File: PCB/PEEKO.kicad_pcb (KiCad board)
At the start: 2 copper layers, 52.1 x 43.2 mm, 32 parts, among them J1 Rasberry PI Pico, J2 Conn_02x15_Odd_Even, J3 Conn_01x02_Pin, J4 Conn_01x02_Pin, U1 TXU0104, U2 TXU0104, U3 TXU0104, U4 TXU0104, U5 TXU0104, U6 TXU0104

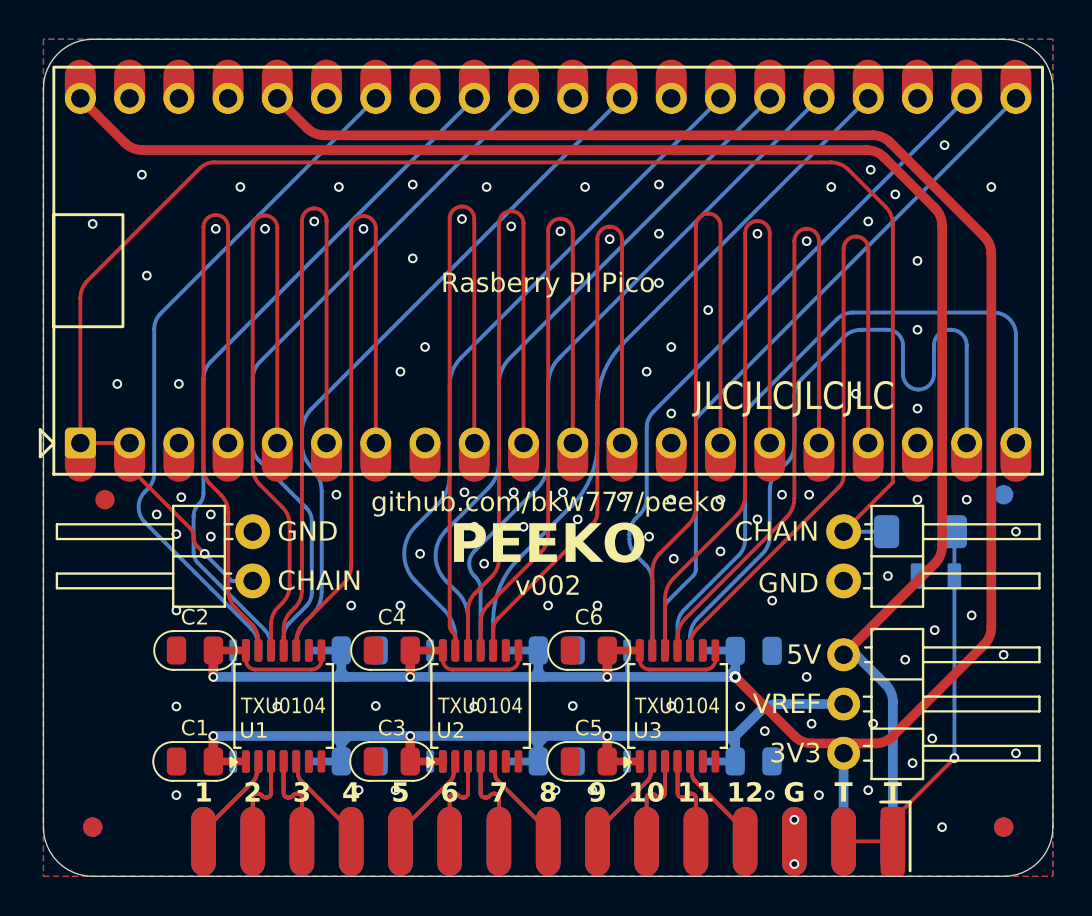
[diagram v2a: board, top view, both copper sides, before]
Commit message: local fiducial footprint
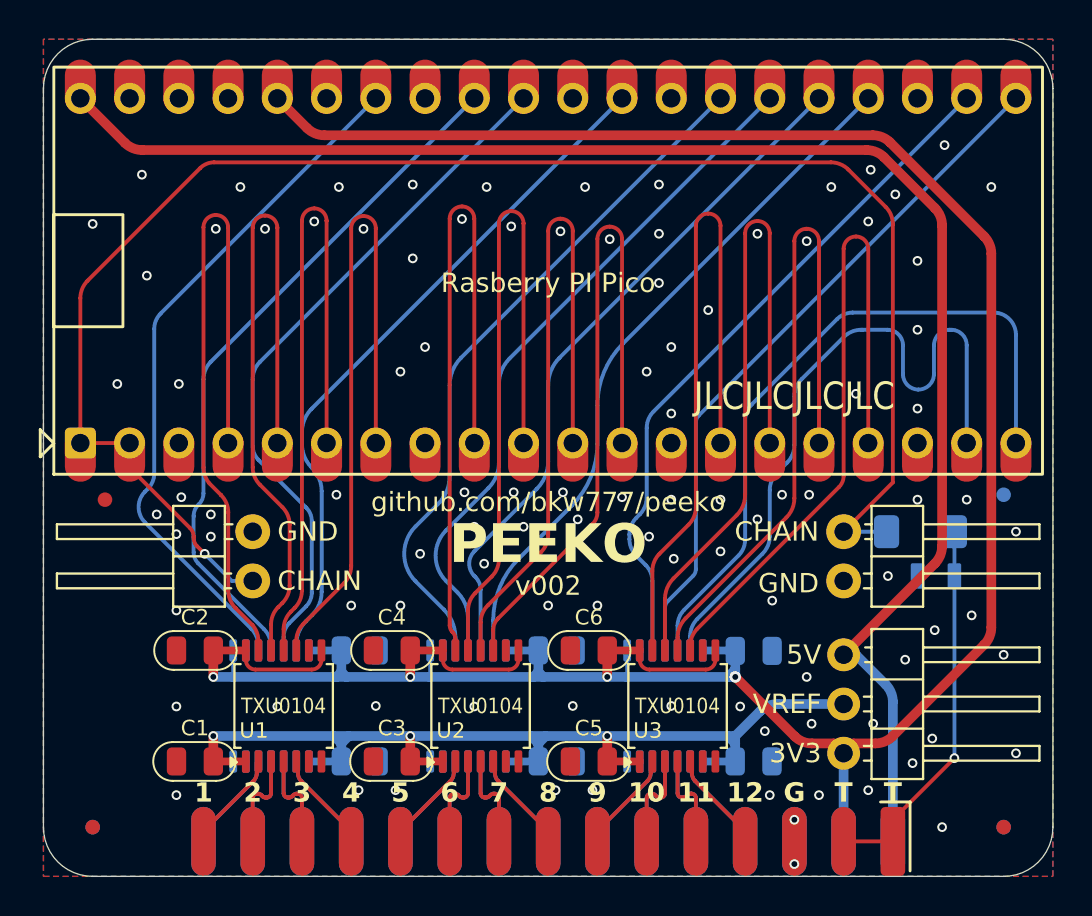
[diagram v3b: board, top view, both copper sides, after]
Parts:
- removed N1: PEEKO housing, 000_LOCAL:PEEKO_housing
- removed the REF** at (169.5, 123.4) (x2)
- removed the REF** at (122.5, 123.4) (x2)
- removed the REF** at (123.2, 106.5)
- removed the REF** at (169.5, 106.3)
- added REF**: Fiducial_1.5, 000_LOCAL:Fiducial_1.5, F.Cu at (169.5, 123.4)
- added REF**: Fiducial_1.5, 000_LOCAL:Fiducial_1.5, F.Cu at (123.2, 106.5)
- added REF**: Fiducial_1.5, 000_LOCAL:Fiducial_1.5, F.Cu at (122.5, 123.4)
- added REF**: Fiducial_1.5, 000_LOCAL:Fiducial_1.5, B.Cu at (122.5, 123.4)
- added REF**: Fiducial_1.5, 000_LOCAL:Fiducial_1.5, B.Cu at (169.5, 123.4)
- added REF**: Fiducial_1.5, 000_LOCAL:Fiducial_1.5, B.Cu at (169.5, 106.3)

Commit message: pics, elecrow assembly bom
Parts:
- added N1: PEEKO housing, 000_LOCAL:PEEKO_housing, F.Cu at (146.0, 104.4)

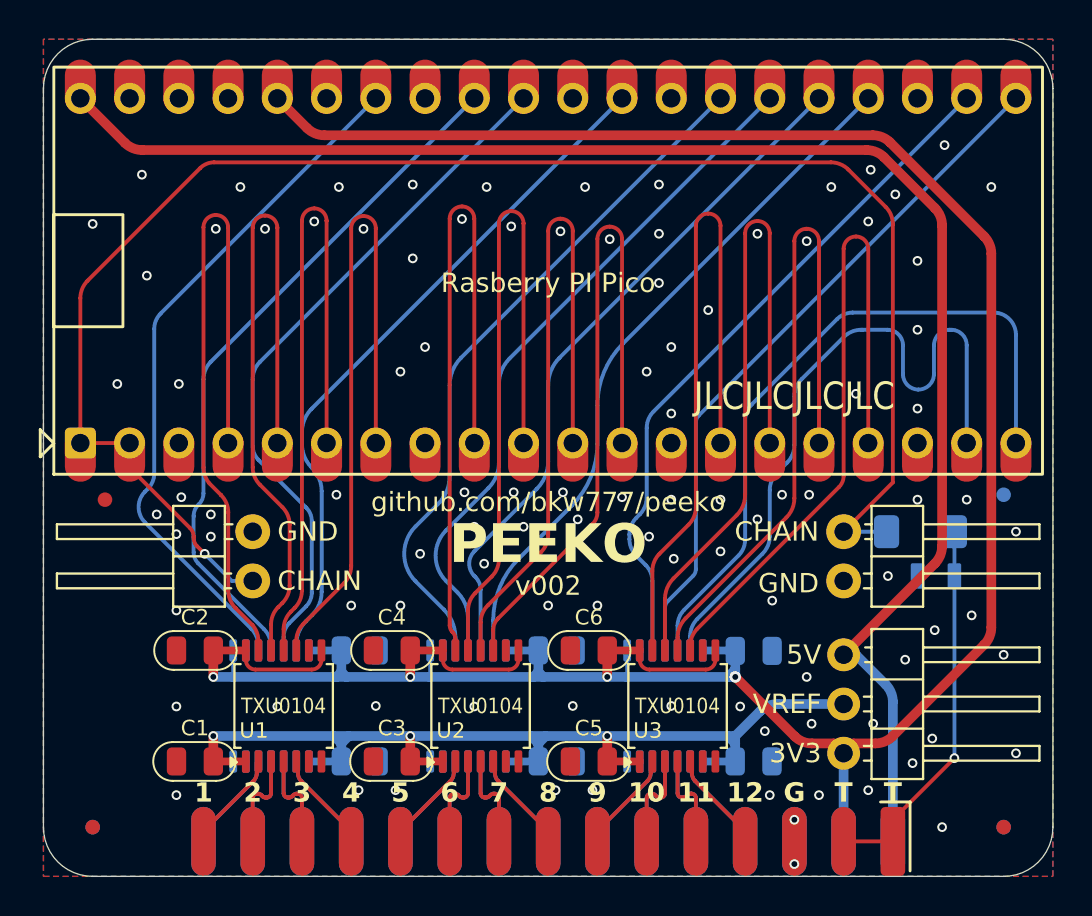
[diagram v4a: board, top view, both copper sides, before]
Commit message: forgotten fillet track on brute
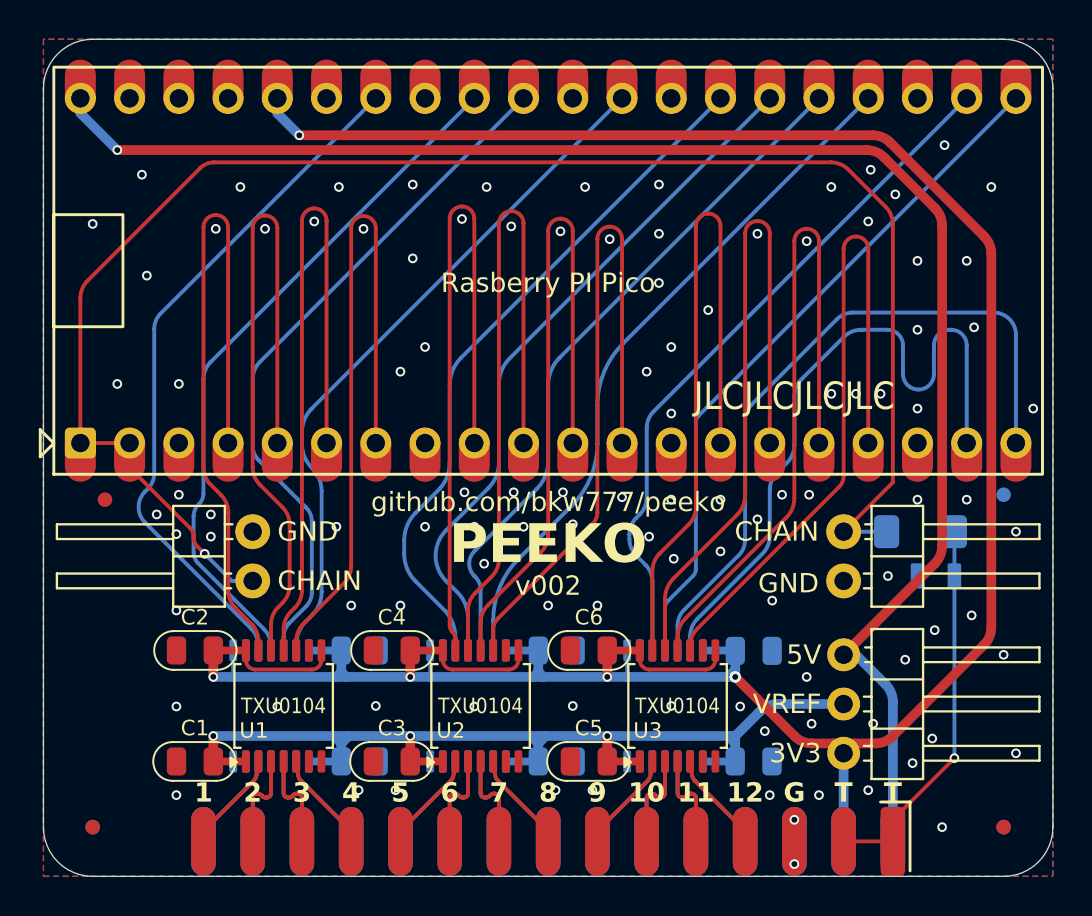
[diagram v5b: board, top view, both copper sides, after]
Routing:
- net +3V3: track 148.7 -> 149.2 mm, vias 4 -> 5
- net +5V: track 82.5 -> 83.0 mm, vias 0 -> 1
- net GND: vias 102 -> 107

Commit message: silkscreen, readme, probe wires, enclosure wall behind pins
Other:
- board text removed: "JLCJLCJLCJLC"

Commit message: shorten chain trace, delete duplicate footprints
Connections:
- J4 pad 1: /CHAIN -> GND
- J4 pad 2: GND -> /CHAIN
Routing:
- net /CHAIN: track 86.0 -> 59.8 mm, vias 1 -> 2
- net GND: track 0.00 -> 4.65 mm, vias 107 -> 109

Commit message: zigzag pi pico dip pins for friction fit
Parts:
- J1: footprint 000_LOCAL:dip-40-700-pi-pico -> 000_LOCAL:dip-40-700-pi-pico-z
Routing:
- net +5V: track 83.0 -> 87.1 mm, vias 1 -> 2
- net +3V3: track 149.2 -> 153.1 mm, vias 5 -> 6
